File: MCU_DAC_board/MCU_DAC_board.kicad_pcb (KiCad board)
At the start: 4 copper layers, 100 x 85 mm, 98 parts, among them J1 Conn_02x04_Odd_Even, J10 Conn_01x03_Pin, J11 105-0752-001, J12 Conn_02x03_Odd_Even, J2 Conn_02x04_Odd_Even, J3 Conn_02x04_Odd_Even, J4 Conn_02x04_Odd_Even, J5 54-00127, J6 105-0752-001, J7 Screw_Terminal_01x02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

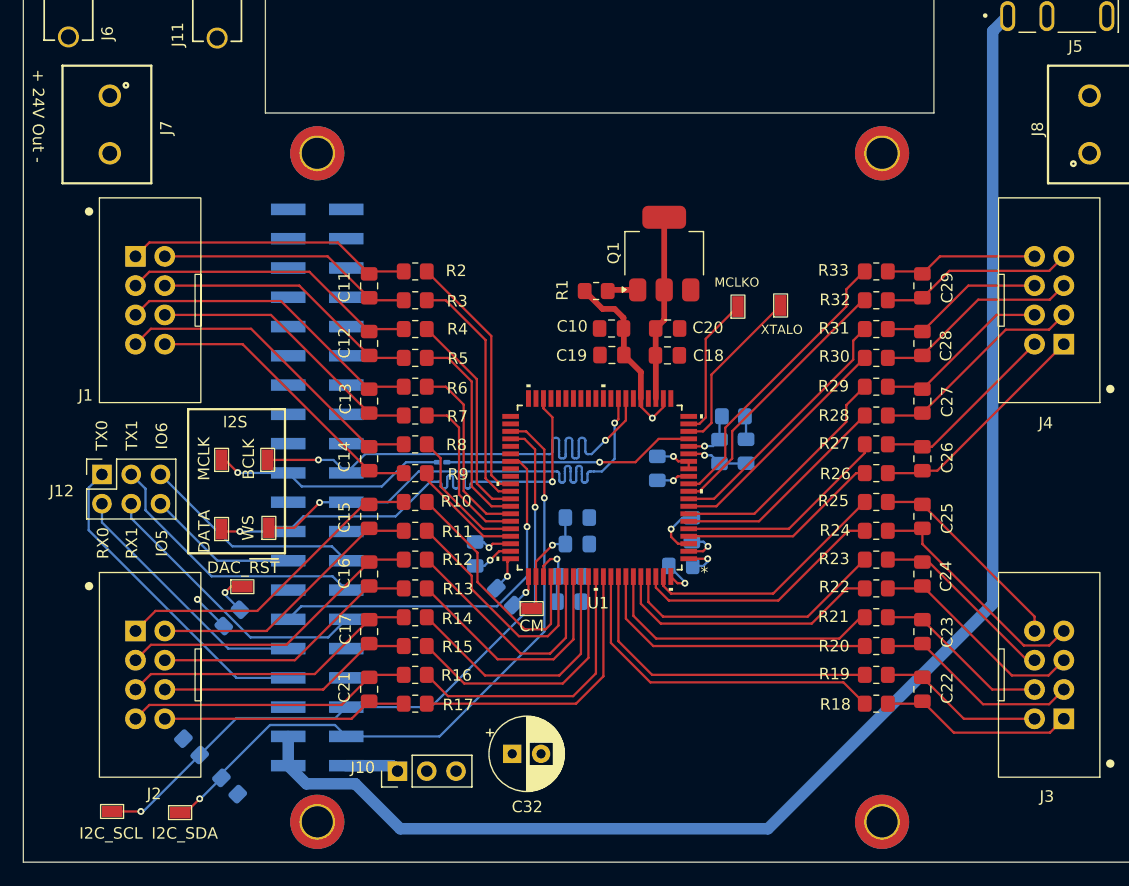
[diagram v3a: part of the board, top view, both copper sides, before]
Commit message: First revision of DAC board
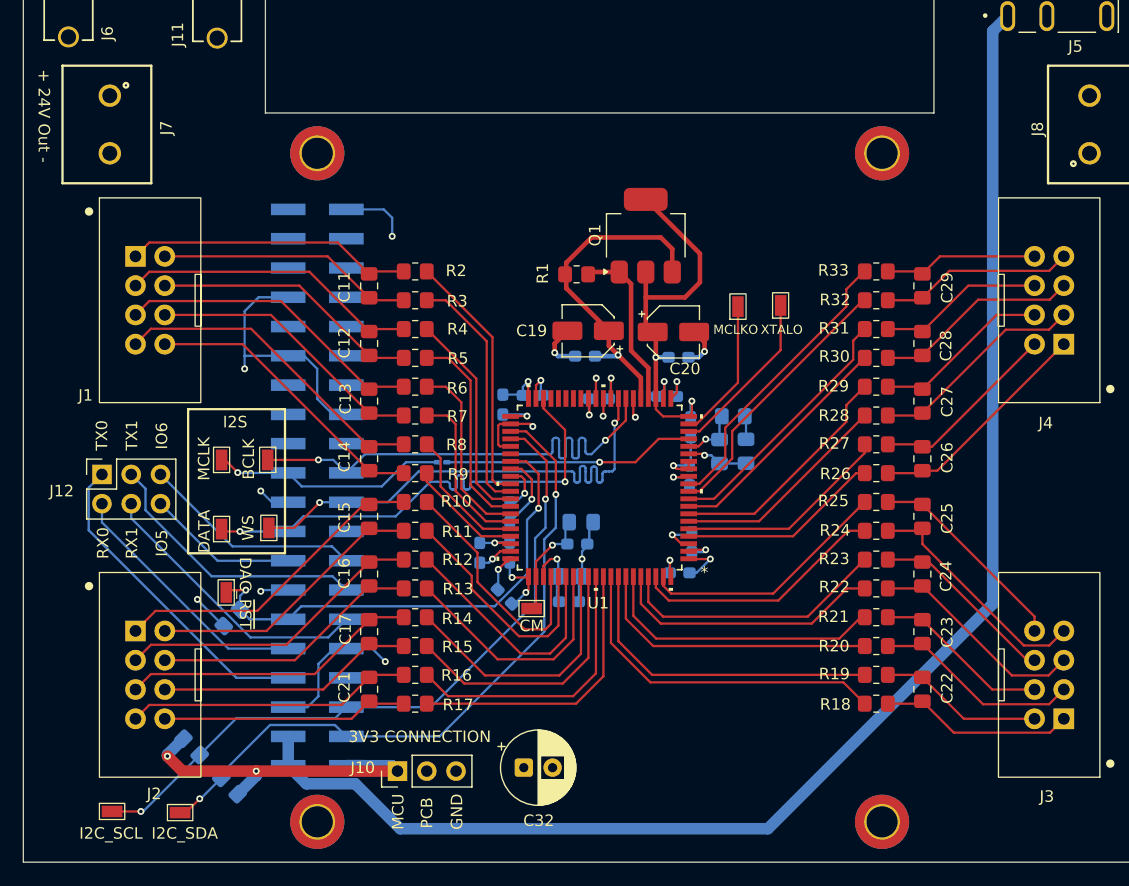
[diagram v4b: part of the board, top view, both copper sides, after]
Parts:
- added C33: 100n, Capacitor_SMD:C_0603_1608Metric_Pad1.08x0.95mm_HandSolder, B.Cu at (125.0, 128.8)
- added C34: 100n, Capacitor_SMD:C_0603_1608Metric_Pad1.08x0.95mm_HandSolder, B.Cu at (140.6, 122.1)
- added C35: 100n, Capacitor_SMD:C_0603_1608Metric_Pad1.08x0.95mm_HandSolder, B.Cu at (138.6, 115.3)
- added C36: 100n, Capacitor_SMD:C_0603_1608Metric_Pad1.08x0.95mm_HandSolder, B.Cu at (127.0, 115.2)
- added C37: 100n, Capacitor_SMD:C_0603_1608Metric_Pad1.08x0.95mm_HandSolder, B.Cu at (140.7, 117.9)
- added C39: 100n, Capacitor_SMD:C_0603_1608Metric_Pad1.08x0.95mm_HandSolder, B.Cu at (132.7, 115.5)
- added C40: 100n, Capacitor_SMD:C_0603_1608Metric_Pad1.08x0.95mm_HandSolder, B.Cu at (124.4, 116.0)
- C1: value 10n -> 100n; footprint Capacitor_SMD:C_0805_2012Metric_Pad1.18x1.45mm_HandSolder -> Capacitor_SMD:C_0603_1608Metric_Pad1.08x0.95mm_HandSolder
- C10, C18: footprint Capacitor_SMD:C_0805_2012Metric_Pad1.18x1.45mm_HandSolder -> Capacitor_SMD:C_0603_1608Metric_Pad1.08x0.95mm_HandSolder; moved to B.Cu
- C19, C20: footprint Capacitor_SMD:C_0805_2012Metric_Pad1.18x1.45mm_HandSolder -> Capacitor_SMD:CP_Elec_4x4.5
- C2, C3, C4, C7, C8, C9: footprint Capacitor_SMD:C_0805_2012Metric_Pad1.18x1.45mm_HandSolder -> Capacitor_SMD:C_0603_1608Metric_Pad1.08x0.95mm_HandSolder
- moved C1 13.4 mm to (125.0, 125.3), turned to -90 degrees
- moved C10 3.32 mm to (131.5, 111.8), turned to 0 degrees
- moved C19 2.94 mm to (131.8, 109.6)
- moved R1 2.23 mm to (130.8, 104.7)
- moved Q1 2.23 mm to (136.8, 101.3)
- moved C32 1.56 mm to (126.2, 147.5)
- moved TP28 1.49 mm to (100.4, 132.3), turned to -90 degrees
- moved C8 1.07 mm to (140.8, 127.9)
- moved C18 0.97 mm to (139.6, 111.9)
- moved C9 0.61 mm to (139.7, 130.6)
- moved C20 0.58 mm to (139.2, 109.7)
- moved C5 0.52 mm to (131.2, 126.2)
- moved C3 0.41 mm to (122.4, 128.8)
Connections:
- C10 pad 1: +3V3 -> GND
- C10 pad 2: GND -> +3V3
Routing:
- net GND: track 10.2 -> 96.0 mm, vias 3 -> 18
- net +2V5: track 21.1 -> 69.0 mm, vias 1 -> 5
- net +3V3: track 30.5 -> 61.7 mm, vias 5 -> 10
- net +3V3_MCU: track 4.63 -> 29.9 mm, vias 0 -> 2
- net /VDRIVE: track 2.64 -> 14.8 mm
- net /DAC_~{RST}: track 37.0 -> 42.5 mm
- net /GPIO8: track 60.0 -> 60.8 mm
- net /GPIO7: track 58.5 -> 59.3 mm
- net Net-(U1-DAC_BIAS3): track 3.36 -> 4.18 mm
- net Net-(U1-DAC_BIAS1): track 3.70 -> 3.09 mm
- net Net-(U1-DAC_BIAS4): track 3.42 -> 2.81 mm
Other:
- board text added: "3V3 CONNECTION"
- board text added: "GND"
- board text added: "MCU"
- board text added: "PCB"

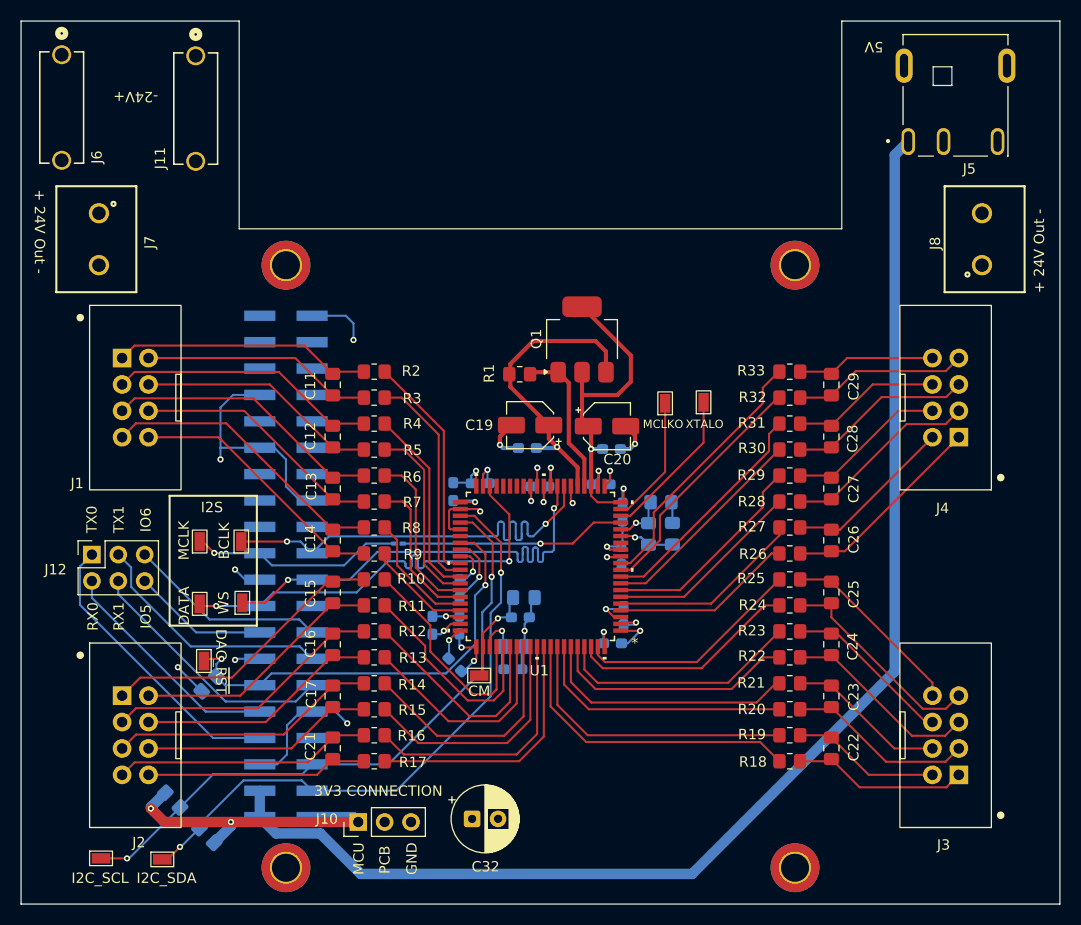
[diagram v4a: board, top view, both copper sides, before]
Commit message: Added via stiching, more decoupling
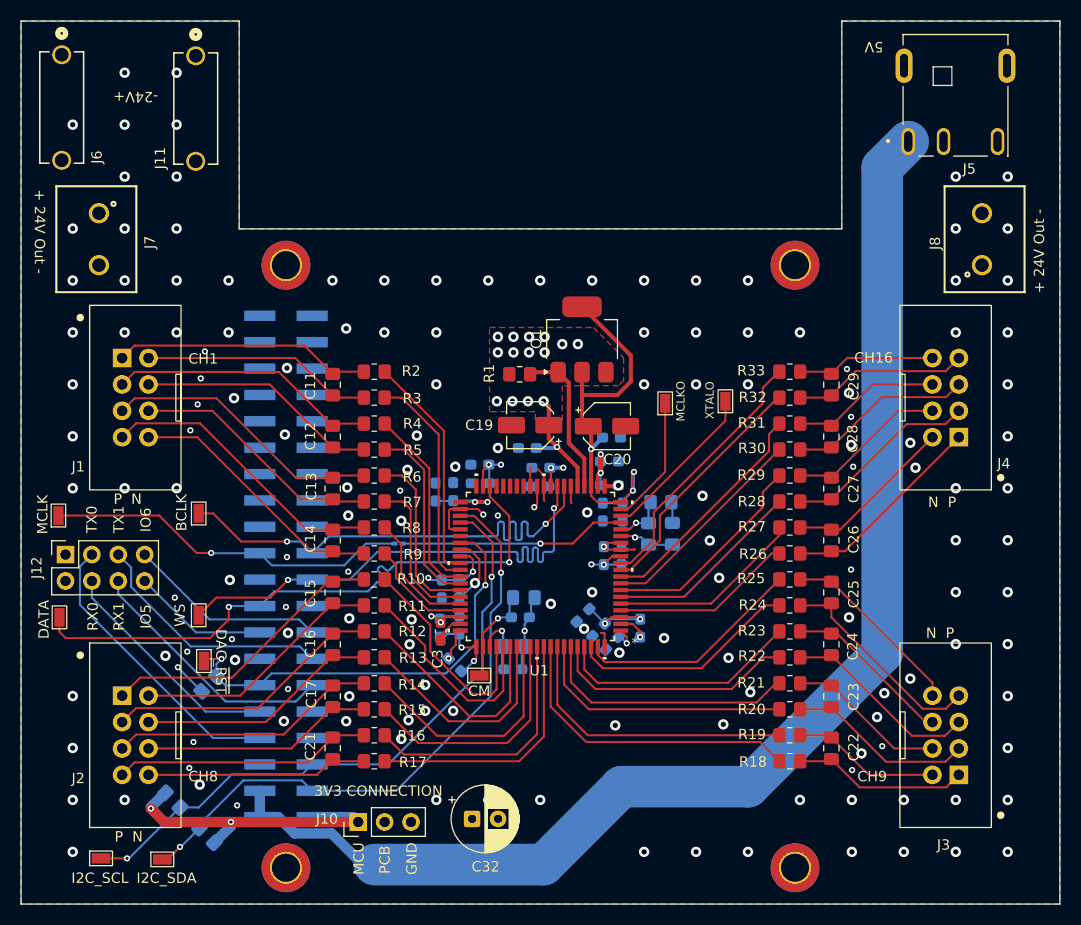
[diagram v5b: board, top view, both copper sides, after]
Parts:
- added C38: 10n, Capacitor_SMD:C_0603_1608Metric_Pad1.08x0.95mm_HandSolder, B.Cu at (123.3, 125.3)
- added C41: 10n, Capacitor_SMD:C_0603_1608Metric_Pad1.08x0.95mm_HandSolder, B.Cu at (123.1, 129.1)
- added C42: 10n, Capacitor_SMD:C_0603_1608Metric_Pad1.08x0.95mm_HandSolder, B.Cu at (138.9, 122.1)
- added C43: 10n, Capacitor_SMD:C_0603_1608Metric_Pad1.08x0.95mm_HandSolder, B.Cu at (138.4, 129.3)
- added C44: 10n, Capacitor_SMD:C_0603_1608Metric_Pad1.08x0.95mm_HandSolder, B.Cu at (136.9, 127.9)
- added C45: 10n, Capacitor_SMD:C_0603_1608Metric_Pad1.08x0.95mm_HandSolder, B.Cu at (122.7, 116.0)
- added C46: 10n, Capacitor_SMD:C_0603_1608Metric_Pad1.08x0.95mm_HandSolder, B.Cu at (132.8, 113.7)
- added C47: 10n, Capacitor_SMD:C_0603_1608Metric_Pad1.08x0.95mm_HandSolder, B.Cu at (138.8, 117.9)
- added C48: 10n, Capacitor_SMD:C_0603_1608Metric_Pad1.08x0.95mm_HandSolder, B.Cu at (126.9, 113.4)
- added C49: 100n, Capacitor_SMD:C_0603_1608Metric_Pad1.08x0.95mm_HandSolder, B.Cu at (139.4, 113.1)
- C3: moved to F.Cu
- J12: value Conn_02x03_Odd_Even -> Conn_02x04_Odd_Even; footprint Connector_PinSocket_2.54mm:PinSocket_2x03_P2.54mm_Vertical -> Connector_PinSocket_2.54mm:PinSocket_2x04_P2.54mm_Vertical
- moved TP2 13.8 mm to (86.4, 118.3)
- moved TP27 13.6 mm to (86.5, 128.1)
- moved TP26 4.91 mm to (99.9, 118.1)
- moved TP3 4.37 mm to (99.9, 127.9)
- moved J12 2.54 mm to (87.1, 122.0)
- moved TP29 2.10 mm to (150.6, 107.3)
- moved C8 2.00 mm to (142.4, 129.1)
- moved C18 1.10 mm to (139.6, 110.8)
- moved C3 0.99 mm to (123.2, 129.4)
- moved C35 0.81 mm to (139.4, 115.4)
- turned C9 to -135 degrees
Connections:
- J12 pad 1: /GPIO37 -> GND
- J12 pad 2: /GPIO38 -> GND
- J12 pad 3: /GPIO20 -> /GPIO37
- J12 pad 4: /GPIO21 -> /GPIO38
- J12 pad 5: /GPIO6 -> /GPIO20
- J12 pad 6: /GPIO5 -> /GPIO21
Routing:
- net GND: track 96.0 -> 39.2 mm, vias 18 -> 159
- net /GPIO4: track 42.6 -> 59.7 mm
- net /GPIO1: track 20.5 -> 35.2 mm
- net +2V5: track 69.0 -> 79.5 mm, vias 5 -> 8
- net /GPIO2: track 44.0 -> 49.3 mm
- net /GPIO3: track 46.0 -> 50.7 mm
- net +5V: track 125.5 -> 123.0 mm
- net Net-(U1-DAC_BIAS3): track 4.18 -> 2.50 mm
- net Net-(U1-XTALO): track 14.8 -> 15.6 mm
- net Net-(U1-DAC_BIAS1): track 3.09 -> 2.69 mm, vias 1 -> 0
- net +3V3: vias 10 -> 30
- added copper zone on F.Cu, net +3V3
- added copper zone on B.Cu, net GND
- added copper zone on F.Cu, net GND
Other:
- board text added: "->"
- board text added: "CH1"
- board text added: "CH16"
- board text added: "CH8"
- board text added: "CH9"
- board text added: "N P"
- board text added: "P N"
- board text removed: "I2S"
